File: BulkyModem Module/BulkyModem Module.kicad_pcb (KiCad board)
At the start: 2 copper layers, 100 x 100 mm, 81 parts, among them J1 DC IN, J2 DCE, J3 Module_Panel, J5 C64_Modem_IDC, K1 HK19F-DC, M1 Mounting, M2 Mounting, M3 Mounting, M4 Mounting, SW1 SET_1200, U1 74HCT244, U2 74HCT04, U3 MAX232, U4 MAX232, U5 74HCT04, U6 74HCT32

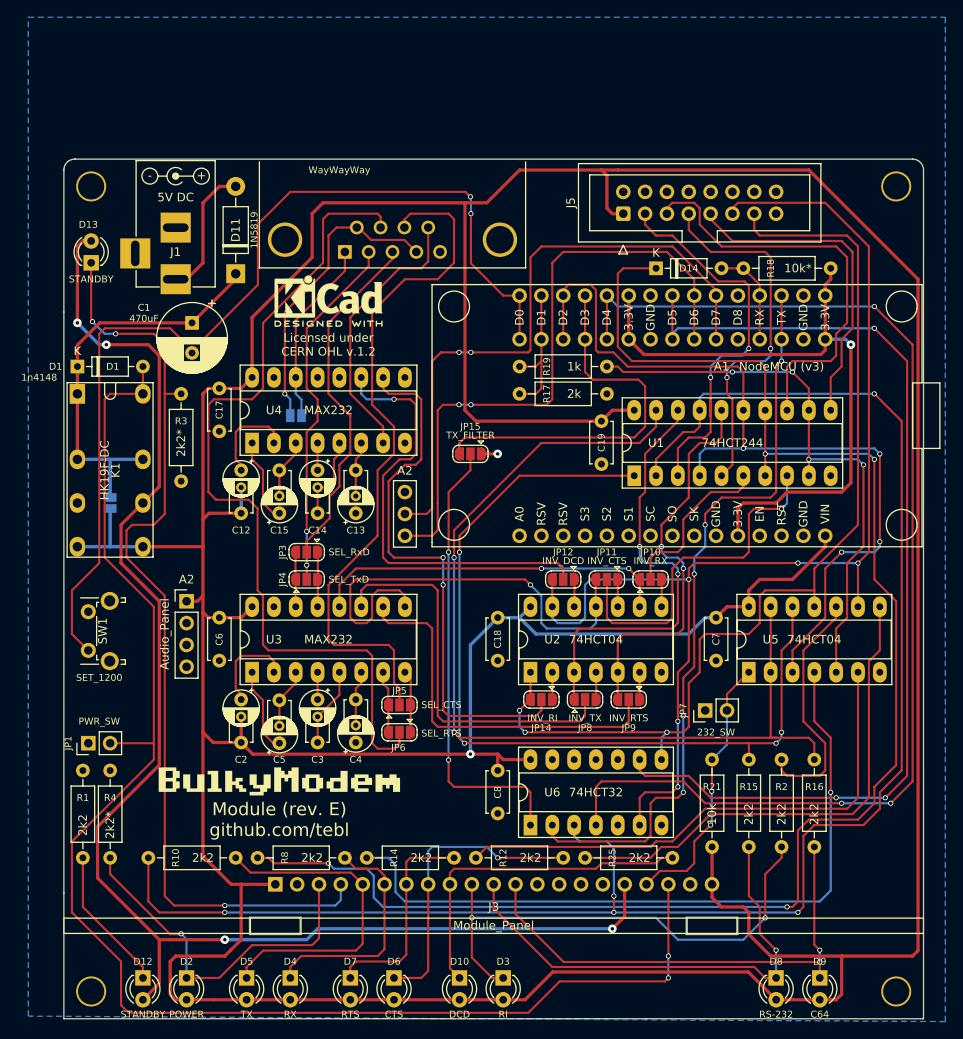
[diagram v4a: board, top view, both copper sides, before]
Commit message: Add labels to LEDs
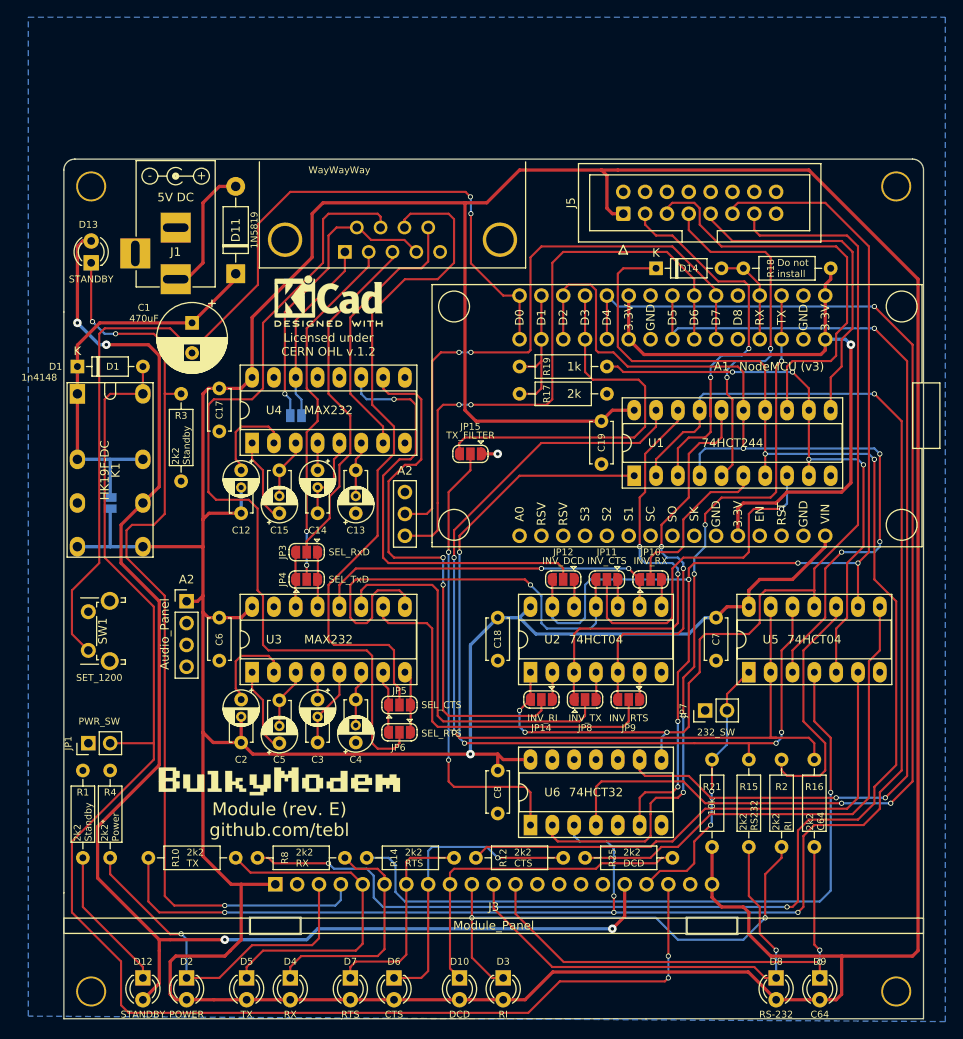
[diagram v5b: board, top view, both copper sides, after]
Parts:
- J5: value C64_Modem_IDC -> C64_Modem_OUT
- R3: value 2k2* -> 2k2
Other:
- board text added: "C64"
- board text added: "CTS"
- board text added: "DCD"
- board text added: "Do not install"
- board text added: "Link JP13 if not installing U4"
- board text added: "Link JP2 if not installing K1"
- board text added: "Power"
- board text added: "RI"
- board text added: "RS232"
- board text added: "RTS"
- board text added: "RX"
- board text added: "Standby"
- board text added: "TX"
